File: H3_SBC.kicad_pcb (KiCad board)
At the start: 6 copper layers, 50 x 40 mm, 167 parts, among them CN1 YXT-BB10-50P-02, CN2 YXT-BB10-50P-02, CN3 YXT-BB10-50P-02, Q1 WPM1481-6/TR, U1 H3, U10 XT28EG32GA4YJECGA, U2 AXP223_C2997893, U5 AP2127K-2.5, U7 MT41K512M16VRP-107 IT:P, U9 RTL8211E-VB-CG, X1 X201232768KLD2SI, X2 SMD-5032_4P 24M 20pf, X3 5YAA25000121TF25E2

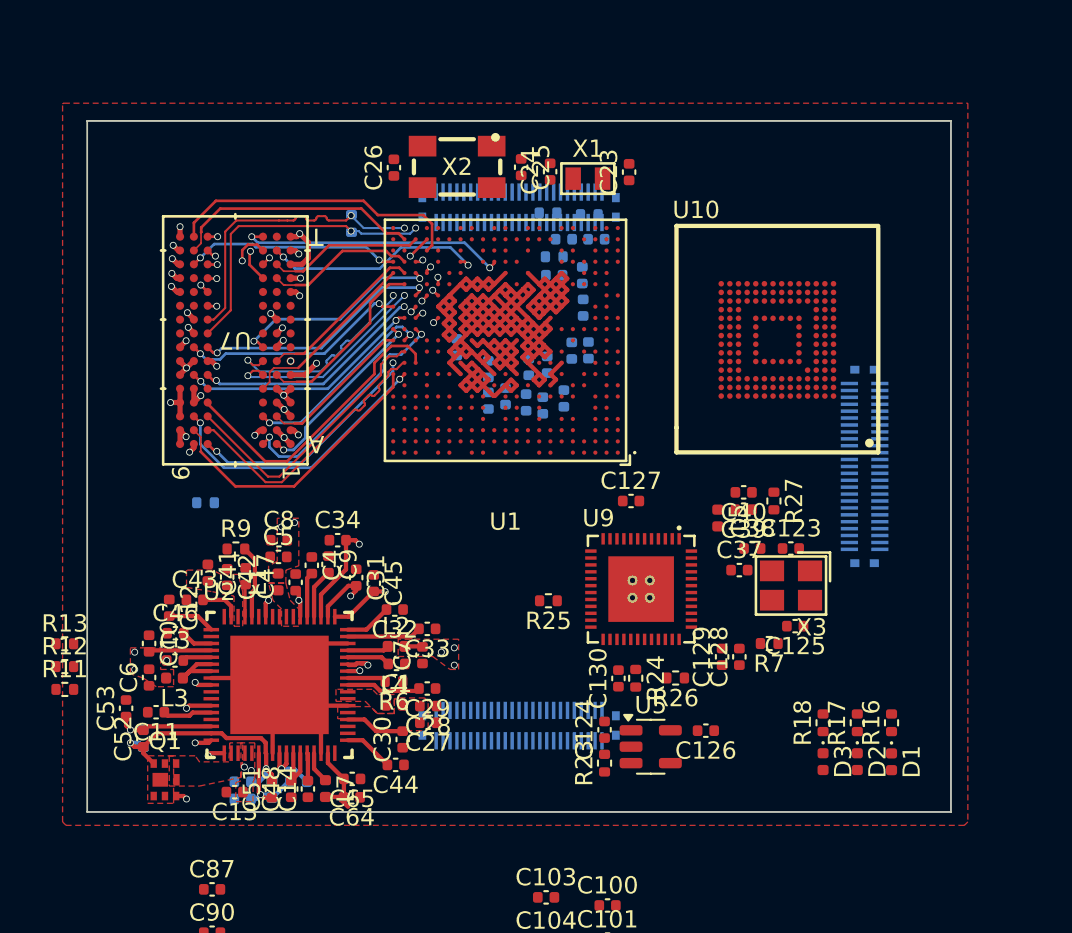
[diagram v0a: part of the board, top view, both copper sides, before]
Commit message: ethernet start and length tuning
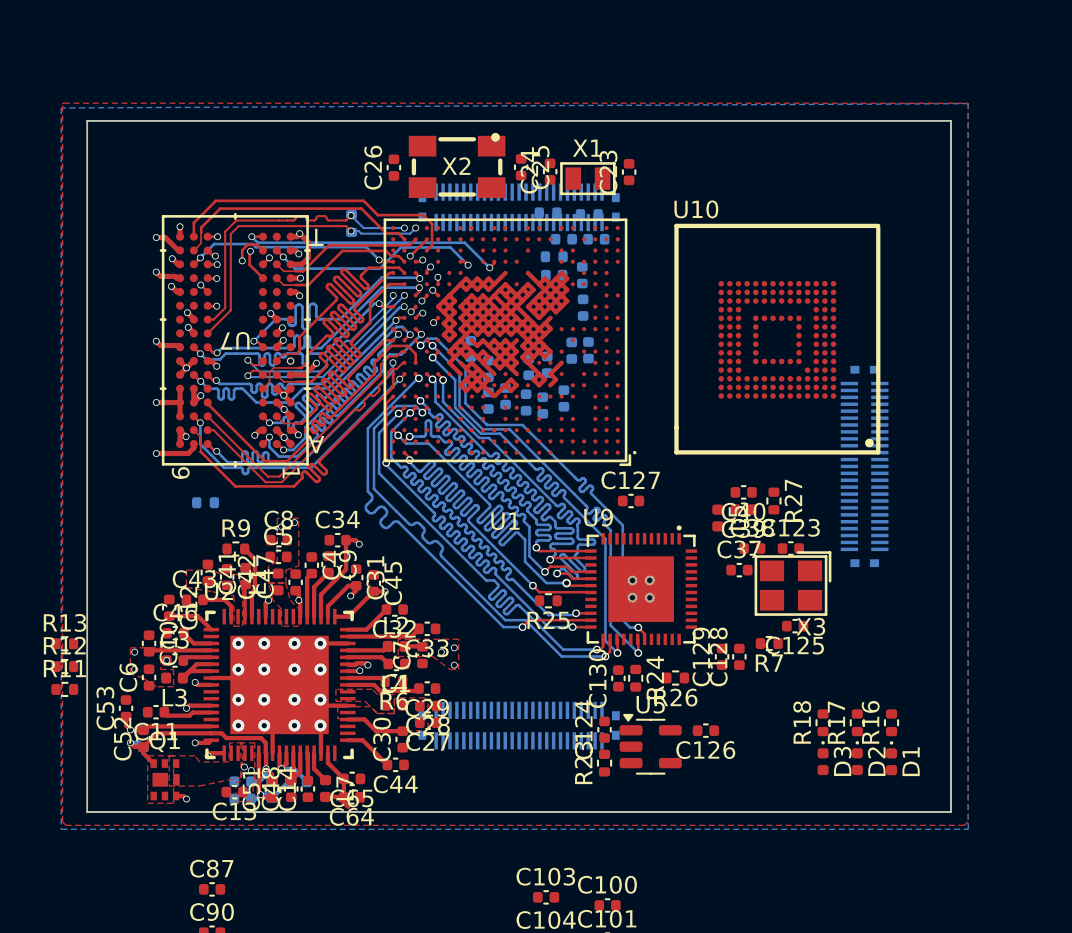
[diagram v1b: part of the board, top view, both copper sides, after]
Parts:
- moved C59 0.81 mm to (122.2, 63.2)
- turned CN3 to 90 degrees
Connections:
- U9 pad : (no net) -> GND
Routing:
- net VCC1V5_DRAM: track 27.5 -> 129.7 mm
- net VCC3V3: track 18.2 -> 88.1 mm
- net RGMII_RXD0: track 0.00 -> 27.2 mm, vias 0 -> 2
- net RGMII_TXD2: track 0.00 -> 26.9 mm, vias 0 -> 2
- net RGMII_MDC: track 0.00 -> 26.9 mm, vias 0 -> 2
- net RGMII_MDIO: track 0.00 -> 26.9 mm, vias 0 -> 2
- net RGMII_TXCTL: track 0.00 -> 26.9 mm, vias 0 -> 2
- net RGMII_TXD3: track 0.00 -> 26.8 mm, vias 0 -> 2
- net RGMII_TXD0: track 0.00 -> 26.8 mm, vias 0 -> 2
- net RGMII_RXD3: track 0.00 -> 26.8 mm, vias 0 -> 2
- net RGMII_RXD2: track 0.00 -> 26.8 mm, vias 0 -> 2
- net RGMII_RXCK: track 0.00 -> 26.8 mm, vias 0 -> 2
- net RGMII_TXD1: track 0.00 -> 26.8 mm, vias 0 -> 2
- net RGMII_RXD1: track 0.00 -> 26.7 mm, vias 0 -> 2
- net RGMII_RXCTL: track 0.00 -> 26.6 mm, vias 0 -> 2
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- added copper zone on B.Cu, net GND

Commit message: more tuning changes
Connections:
- U9 pad : GND -> (no net)
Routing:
- net /Ethernet/CKXTAL_IN: track 0.00 -> 8.78 mm
- net /Ethernet/CKXTAL_OUT: track 0.00 -> 6.71 mm
- net GND: track 103.9 -> 108.0 mm

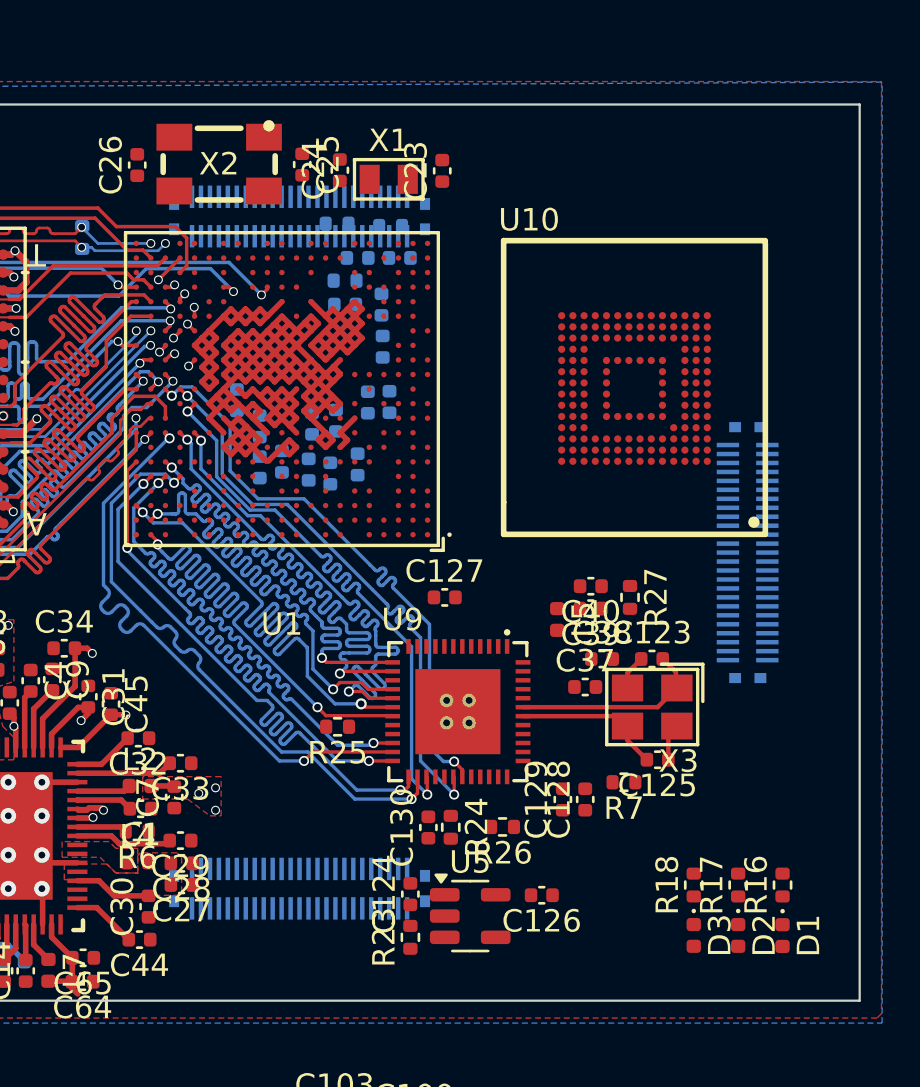
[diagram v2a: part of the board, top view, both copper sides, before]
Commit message: routed ethernet and emmc data lines
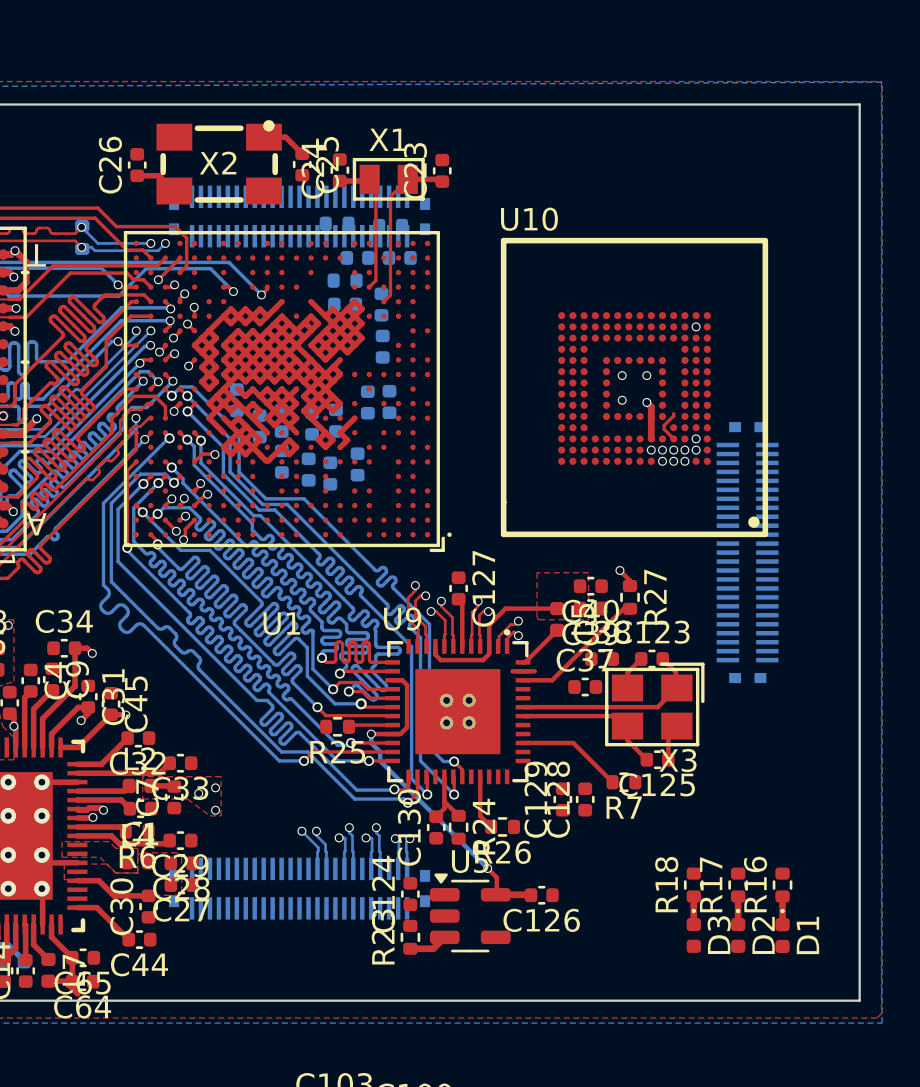
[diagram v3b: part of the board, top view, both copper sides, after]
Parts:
- moved C36 2.29 mm to (124.2, 64.1), turned to -90 degrees
- moved C127 0.74 mm to (132.1, 71.6), turned to -90 degrees
- moved C130 0.35 mm to (131.1, 82.3)
- moved R24 0.35 mm to (132.1, 82.3)
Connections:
- U9 pad : (no net) -> GND
- U9 pad 15: unconnected-(U9-DVDD33-Pad15) -> /Ethernet/DVDD25
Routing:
- net VCC3V3: track 88.1 -> 56.2 mm, vias 3 -> 4
- net /Storage/EMMC_DQ5: track 0.00 -> 31.6 mm, vias 0 -> 2
- net /Storage/EMMC_DQ4: track 0.00 -> 31.5 mm, vias 0 -> 2
- net /Storage/EMMC_DQ3: track 0.00 -> 31.5 mm, vias 0 -> 2
- net /Storage/EMMC_DQ6: track 0.00 -> 31.5 mm, vias 0 -> 2
- net /Storage/EMMC_DQ0: track 0.00 -> 31.5 mm, vias 0 -> 2
- net /Storage/EMMC_DQ7: track 0.00 -> 31.5 mm, vias 0 -> 2
- net /Storage/EMMC_DQ1: track 0.00 -> 31.5 mm, vias 0 -> 2
- net /Storage/EMMC_DQ2: track 0.00 -> 31.4 mm, vias 0 -> 2
- net RGMII_CLKIN: track 0.00 -> 24.2 mm, vias 0 -> 2
- net ENET_MDI3-: track 0.00 -> 23.4 mm, vias 0 -> 2
- net ENET_MDI2+: track 0.00 -> 23.3 mm, vias 0 -> 2
- net ENET_MDI3+: track 0.00 -> 23.3 mm, vias 0 -> 2
- net ENET_MDI0-: track 0.00 -> 23.3 mm, vias 0 -> 2
- net ENET_MDI2-: track 0.00 -> 23.3 mm, vias 0 -> 2
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- added copper zone on F.Cu, net /Ethernet/AVDD10

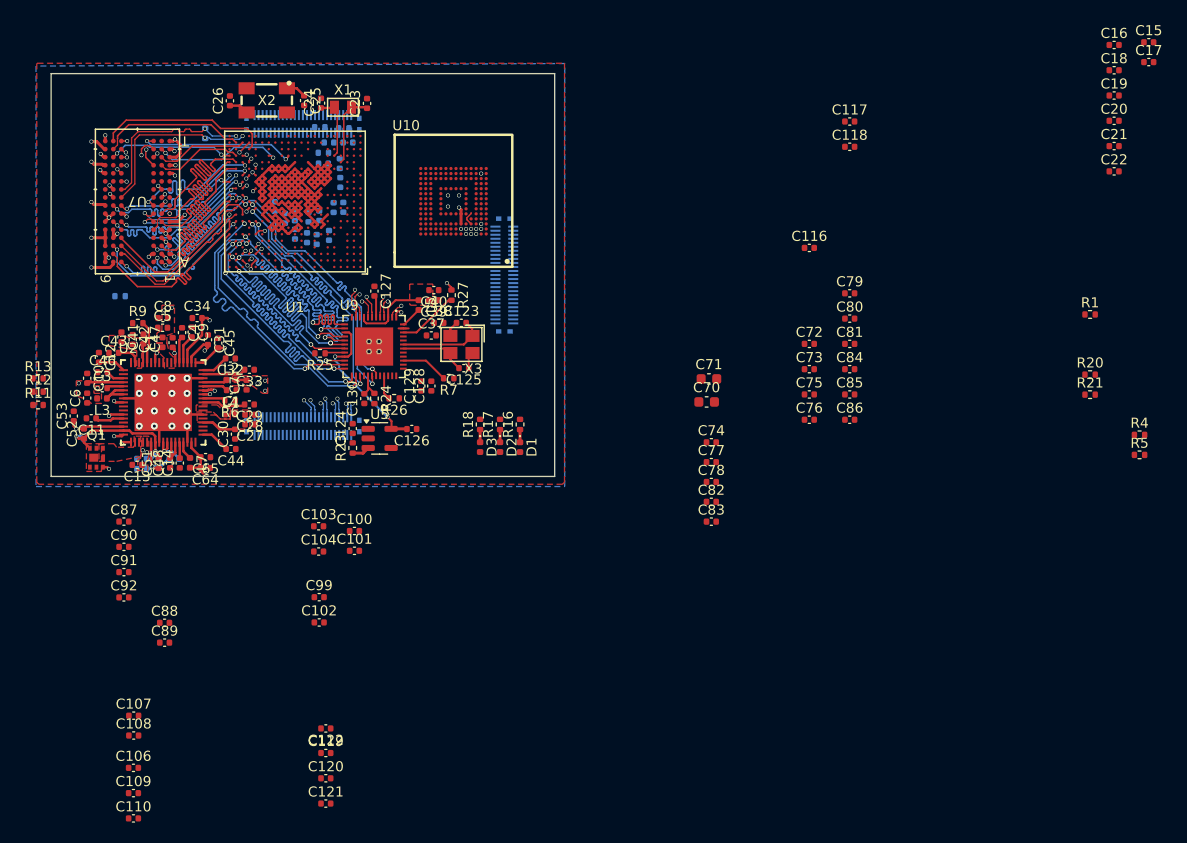
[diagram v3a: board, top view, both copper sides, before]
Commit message: placed all decaps, emmc routing changes, DDR routing changes
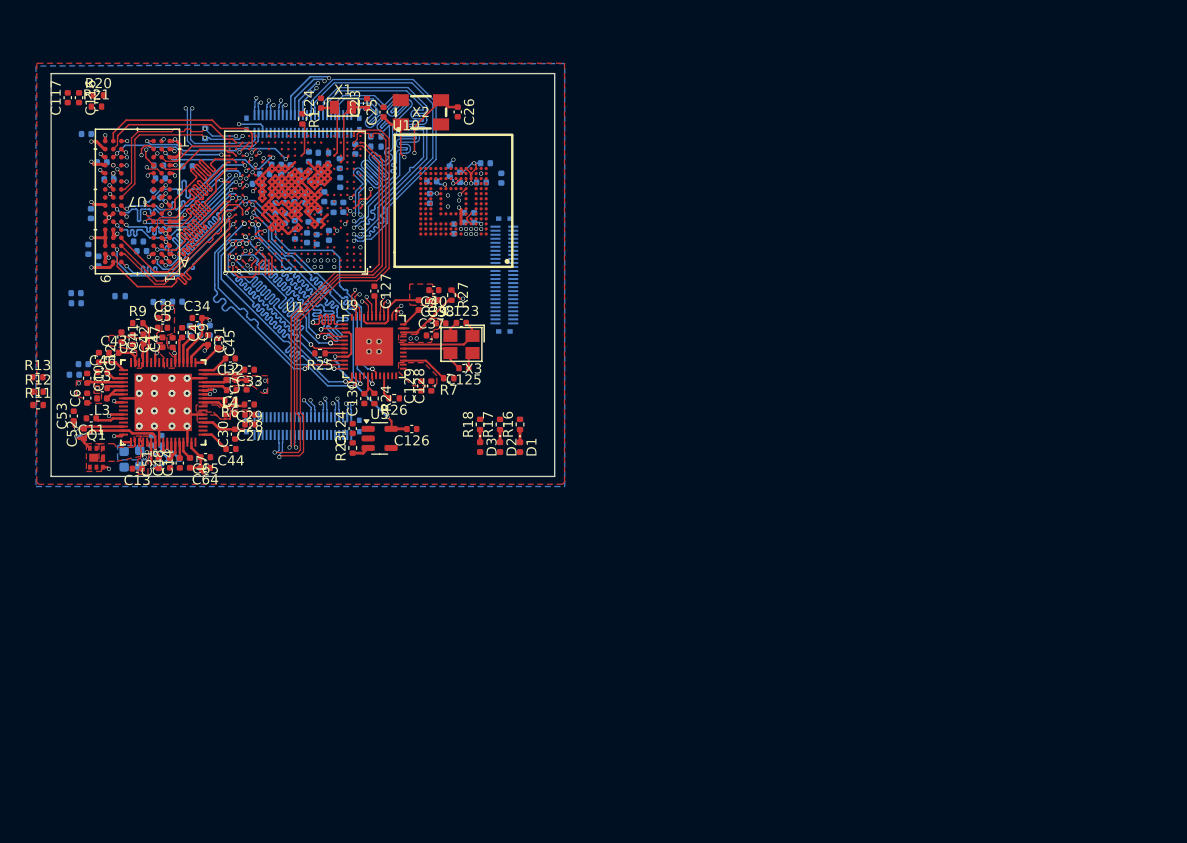
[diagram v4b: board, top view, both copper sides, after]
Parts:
- removed C121, C122: 0.1uF, Capacitor_SMD:C_0402_1005Metric
- removed C72: 10uF, Capacitor_SMD:C_0402_1005Metric
- C100, C101, C102, C103, C104, C106, C107, C108, C109, C110, C118, C119, C120, C15, C16, C17, C18, C19, C20, C21, C22, C70, C71, C73, C74, C75, C76, C77, C78, C79, C80, C81, C82, C83, C84, C85, C86, C87, C88, C89, C90, C91, C92, C99, R4, R5: moved to B.Cu
- moved R21 102.7 mm to (104.5, 53.3)
- moved R20 102.3 mm to (104.7, 52.1)
- moved R1 80.6 mm to (125.0, 54.5), turned to -90 degrees
- moved C117 77.7 mm to (101.7, 52.4), turned to 90 degrees
- moved C85 76.2 mm to (103.2, 78.8)
- moved R5 74.1 mm to (139.6, 59.7), turned to -90 degrees
- moved C116 74.0 mm to (102.8, 52.4), turned to -90 degrees
- moved R4 72.2 mm to (140.6, 60.3), turned to -90 degrees
- moved C15 70.2 mm to (141.0, 64.3), turned to 90 degrees
- moved C21 68.1 mm to (137.6, 62.4), turned to -90 degrees
- moved C22 67.8 mm to (137.8, 60.7), turned to 180 degrees
- moved C80 66.8 mm to (112.5, 72.7)
- moved C20 66.4 mm to (140.0, 65.4), turned to -90 degrees
- moved C16 65.8 mm to (142.0, 64.3), turned to 90 degrees
- moved C17 65.3 mm to (144.7, 60.4), turned to 90 degrees
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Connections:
- CN1 pad 1: HTX0- -> HTX2-
- CN1 pad 10: HTXC- -> HTXC+
- CN1 pad 11: HTXC+ -> HTXC-
- CN1 pad 18: PG0 -> USB1_D+
- CN1 pad 19: PG1 -> USB1_D-
- CN1 pad 2: HTX0+ -> HTX2+
- CN1 pad 20: PG2 -> GND
- CN1 pad 21: PG3 -> USB2_D+
- CN1 pad 22: PG4 -> USB2_D-
- CN1 pad 23: PG5 -> GND
- CN1 pad 24: PG6 -> USB3_D+
- CN1 pad 25: PG7 -> USB3_D-
- CN1 pad 26: CHG_LED -> USB0_D-
- CN1 pad 27: GND -> USB0_D+
- CN1 pad 28: GND -> USB0_ID
- CN1 pad 29: SDC0_DET -> GND
- CN1 pad 30: SDC0_CMD -> CHG_LED
- CN1 pad 31: SDC0_CLK -> GND
- CN1 pad 33: SDC0_D3 -> SDC0_DET
- CN1 pad 34: SDC0_D2 -> SDC0_CMD
- CN1 pad 35: GND -> SDC0_CLK
- CN1 pad 36: SDC0_D1 -> GND
- CN1 pad 37: SDC0_D0 -> SDC0_D3
- CN1 pad 38: GND -> SDC0_D2
- CN1 pad 39: USB3_D+ -> GND
- CN1 pad 4: HTX1- -> HTX1+
- CN1 pad 40: USB2_D+ -> SDC0_D1
- CN1 pad 41: GND -> SDC0_D0
- CN1 pad 42: USB1_D+ -> GND
- CN1 pad 43: USB0_D+ -> PG7
- CN1 pad 44: GND -> PG6
- CN1 pad 45: USB3_D- -> PG5
- CN1 pad 46: USB2_D- -> PG4
- CN1 pad 47: GND -> PG3
- CN1 pad 48: USB0_ID -> PG2
- CN1 pad 49: USB1_D- -> PG1
- CN1 pad 5: HTX1+ -> HTX1-
- CN1 pad 50: USB0_D- -> PG0
- CN1 pad 7: HTX2- -> HTX0+
- CN1 pad 8: HTX2+ -> HTX0-
- U1 pad AA11: SDQ25 -> unconnected-(U1C-SDQ25-PadAA11)
- U1 pad AA12: /RAM/SDQM3 -> unconnected-(U1C-SDQM3-PadAA12)
- U1 pad AA14: SDQ21 -> unconnected-(U1C-SDQ21-PadAA14)
- U1 pad AA15: /RAM/SDQS2+ -> unconnected-(U1C-SDQS2-PadAA15)
- U1 pad AA17: SDQ17 -> unconnected-(U1C-SDQ17-PadAA17)
- U1 pad AA18: /RAM/SDQM2 -> unconnected-(U1C-SDQM2-PadAA18)
- U1 pad AA8: SDQ29 -> unconnected-(U1C-SDQ29-PadAA8)
- U1 pad AA9: /RAM/SDQS3+ -> unconnected-(U1C-SDQS3-PadAA9)
- U1 pad W12: SDQ24 -> unconnected-(U1C-SDQ24-PadW12)
- U1 pad W15: SDQ19 -> unconnected-(U1C-SDQ19-PadW15)
- U1 pad W9: SDQ28 -> unconnected-(U1C-SDQ28-PadW9)
- U1 pad Y10: SDQ27 -> unconnected-(U1C-SDQ27-PadY10)
- U1 pad Y11: SDQ26 -> unconnected-(U1C-SDQ26-PadY11)
- U1 pad Y12: SDQ23 -> unconnected-(U1C-SDQ23-PadY12)
- U1 pad Y13: SDQ22 -> unconnected-(U1C-SDQ22-PadY13)
- U1 pad Y14: SDQ20 -> unconnected-(U1C-SDQ20-PadY14)
- U1 pad Y15: /RAM/SDQS2- -> unconnected-(U1C-SDQS2B-PadY15)
- U1 pad Y16: SDQ18 -> unconnected-(U1C-SDQ18-PadY16)
- U1 pad Y17: SDQ16 -> unconnected-(U1C-SDQ16-PadY17)
- U1 pad Y7: SDQ31 -> unconnected-(U1C-SDQ31-PadY7)
- U1 pad Y8: SDQ30 -> unconnected-(U1C-SDQ30-PadY8)
- U1 pad Y9: /RAM/SDQS3- -> unconnected-(U1C-SDQS3B-PadY9)
- U9 pad : GND -> (no net)
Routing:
- net MICIN_2-: track 0.00 -> 46.3 mm, vias 0 -> 1
- net MICIN_2+: track 0.00 -> 46.2 mm, vias 0 -> 1
- net Net-(U1H-PC5/NAND_RE): track 0.00 -> 45.5 mm, vias 0 -> 2
- net USB0_D+: track 0.00 -> 39.6 mm, vias 0 -> 2
- net USB0_D-: track 0.00 -> 39.6 mm, vias 0 -> 2
- net MICIN_1+: track 0.00 -> 38.7 mm, vias 0 -> 1
- net MICIN_1-: track 0.00 -> 38.7 mm, vias 0 -> 1
- net /Storage/EMMC_CMD: track 0.00 -> 34.6 mm, vias 0 -> 2
- net HSCL: track 0.00 -> 33.9 mm, vias 0 -> 2
- net HSDA: track 0.00 -> 33.9 mm, vias 0 -> 2
- net HTX0-: track 0.00 -> 33.9 mm, vias 0 -> 1
- net HCEC: track 0.00 -> 33.9 mm, vias 0 -> 2
- net HHPD: track 0.00 -> 33.9 mm, vias 0 -> 2
- net HTXC-: track 0.00 -> 33.8 mm, vias 0 -> 1
- net HTX1-: track 0.00 -> 33.8 mm, vias 0 -> 1
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- added copper zone on B.Cu, net +5V
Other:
- board text added: "Layout later (SVREF voltage divider)"
